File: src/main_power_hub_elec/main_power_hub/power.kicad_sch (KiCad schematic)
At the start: 35 parts, among them J1 XT30M, U220 MP2459GJ-Z-MS, U230 AP62200TWU, U240 HX4002

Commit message: Wire channels on schematic
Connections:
- net VBUS_{SENSE}: now also C12.2, R3.2, R4.1
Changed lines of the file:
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@@
+	)
+	(junction
+		(at 73.66 36.83)
+		(diameter 0)
+		(color 0 0 0 0)
 	)
 	(junction
@@
 		)
 		(stroke
+			(width 0)
+			(type default)
+		)
+	)
+	(wire
+		(pts
+			(xy 73.66 36.83) (xy 76.2 36.83)
+		)
+		(stroke

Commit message: Make the bus real
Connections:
- net +12V: no longer U230.5 (EN)
- net GND: now also D3.2 (A2); no longer D3.1 (A1)
- net VBUS: now also D3.1 (A1); no longer D3.2 (A2)
- no-connect marks 0 -> 1
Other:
- moved on the sheet: D3
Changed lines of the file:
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@@
 	)
 	(junction
-		(at 29.21 81.28)
-		(diameter 0)
-		(color 0 0 0 0)
-	)
-	(junction
 		(at 185.42 39.37)
 		(diameter 0)
@@
 		(color 0 0 0 0)
 	)
+	(no_connect
+		(at 30.48 86.36)
+	)
 	(wire
 		(pts
@@
 	(wire
 		(pts
-			(xy 30.48 86.36) (xy 29.21 86.36)
-		)
-		(stroke
-			(width 0)
-			(type default)
-		)
-	)
-	(wire
-		(pts
 			(xy 34.29 133.35) (xy 36.83 133.35)
 		)
@@
 	(wire
 		(pts
-			(xy 29.21 81.28) (xy 30.48 81.28)
+			(xy 26.67 81.28) (xy 30.48 81.28)
 		)
 		(stroke
@@
 	(wire
 		(pts
-			(xy 29.21 81.28) (xy 29.21 86.36)
-		)
-		(stroke
-			(width 0)
-			(type default)
-		)
-	)
-	(wire
-		(pts
 			(xy 185.42 35.56) (xy 185.42 39.37)
 		)
@@
 	(wire
 		(pts
-			(xy 26.67 81.28) (xy 29.21 81.28)
-		)
-		(stroke
-			(width 0)
-			(type default)
-		)
-	)
-	(wire
-		(pts
 			(xy 195.58 26.67) (xy 199.39 26.67)
 		)
@@
 	(symbol
 		(lib_id "Device:D_TVS_Small")
-		(at 55.88 33.02 90)
+		(at 55.88 33.02 270)
 		(unit 1)
 		(exclude_from_sim no)
@@
 		(dnp no)
 		(property "Reference" "D3"
-			(at 57.912 33.02 90)
+			(at 53.848 33.02 90)
 			(effects
 				(font
@@
 		)
 		(property "Value" "30V"
-			(at 57.912 35.56 90)
+			(at 53.848 30.48 90)
 			(effects
 				(font

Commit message: Schematic done (?)
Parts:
- J1: value XT30M -> XT90M

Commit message: evan made me do it footprints done
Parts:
- C12: footprint (none) -> Capacitor_SMD:C_0402_1005Metric
- D3: footprint (none) -> Diode_SMD:D_SMF
- J1: footprint (none) -> Connector_AMASS:AMASS_XT90PW-M_1x02_P10.90mm_Horizontal
- R3, R4: footprint (none) -> Resistor_SMD:R_0402_1005Metric
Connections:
- net VBUS_{FLT}: no longer U220.4 (EN)
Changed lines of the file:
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@@
 	)
 	(junction
-		(at 148.59 26.67)
-		(diameter 0)
-		(color 0 0 0 0)
-	)
-	(junction
 		(at 190.5 39.37)
 		(diameter 0)
@@
 	(wire
 		(pts
-			(xy 148.59 26.67) (xy 146.05 26.67)
+			(xy 146.05 26.67) (xy 149.86 26.67)
 		)
 		(stroke
@@
 	(wire
 		(pts
-			(xy 148.59 26.67) (xy 149.86 26.67)
-		)
-		(stroke
-			(width 0)
-			(type default)
-		)
-	)
-	(wire
-		(pts
 			(xy 34.29 133.35) (xy 36.83 133.35)
 		)
@@
 	(wire
 		(pts
-			(xy 149.86 31.75) (xy 148.59 31.75)
-		)
-		(stroke
-			(width 0)
-			(type default)
-		)
-	)
-	(wire
-		(pts
 			(xy 58.42 81.28) (xy 58.42 83.82)
 		)
@@
 	(wire
 		(pts
-			(xy 148.59 26.67) (xy 148.59 31.75)
-		)
-		(stroke
-			(width 0)
-			(type default)
-		)
-	)
-	(wire
-		(pts
 			(xy 53.34 86.36) (xy 50.8 86.36)
 		)
@@
 			)
 		)
-		(property "Footprint" ""
+		(property "Footprint" "Capacitor_SMD:C_0402_1005Metric"
 			(at 73.66 43.18 90)
 			(effects
@@
 			)
 		)
-		(property "Footprint" ""
+		(property "Footprint" "Connector_AMASS:AMASS_XT90PW-M_1x02_P10.90mm_Horizontal"
 			(at 30.48 29.21 0)
 			(effects
@@
 			)
 		)
-		(property "Footprint" ""
+		(property "Footprint" "Resistor_SMD:R_0402_1005Metric"
 			(at 67.31 41.91 0)
 			(effects
@@
 			)
 		)
-		(property "Footprint" ""
+		(property "Footprint" "Diode_SMD:D_SMF"
 			(at 55.88 33.02 0)
 			(effects
@@
 			)
 		)
-		(property "Footprint" ""
+		(property "Footprint" "Resistor_SMD:R_0402_1005Metric"
 			(at 67.31 33.02 0)
 			(effects

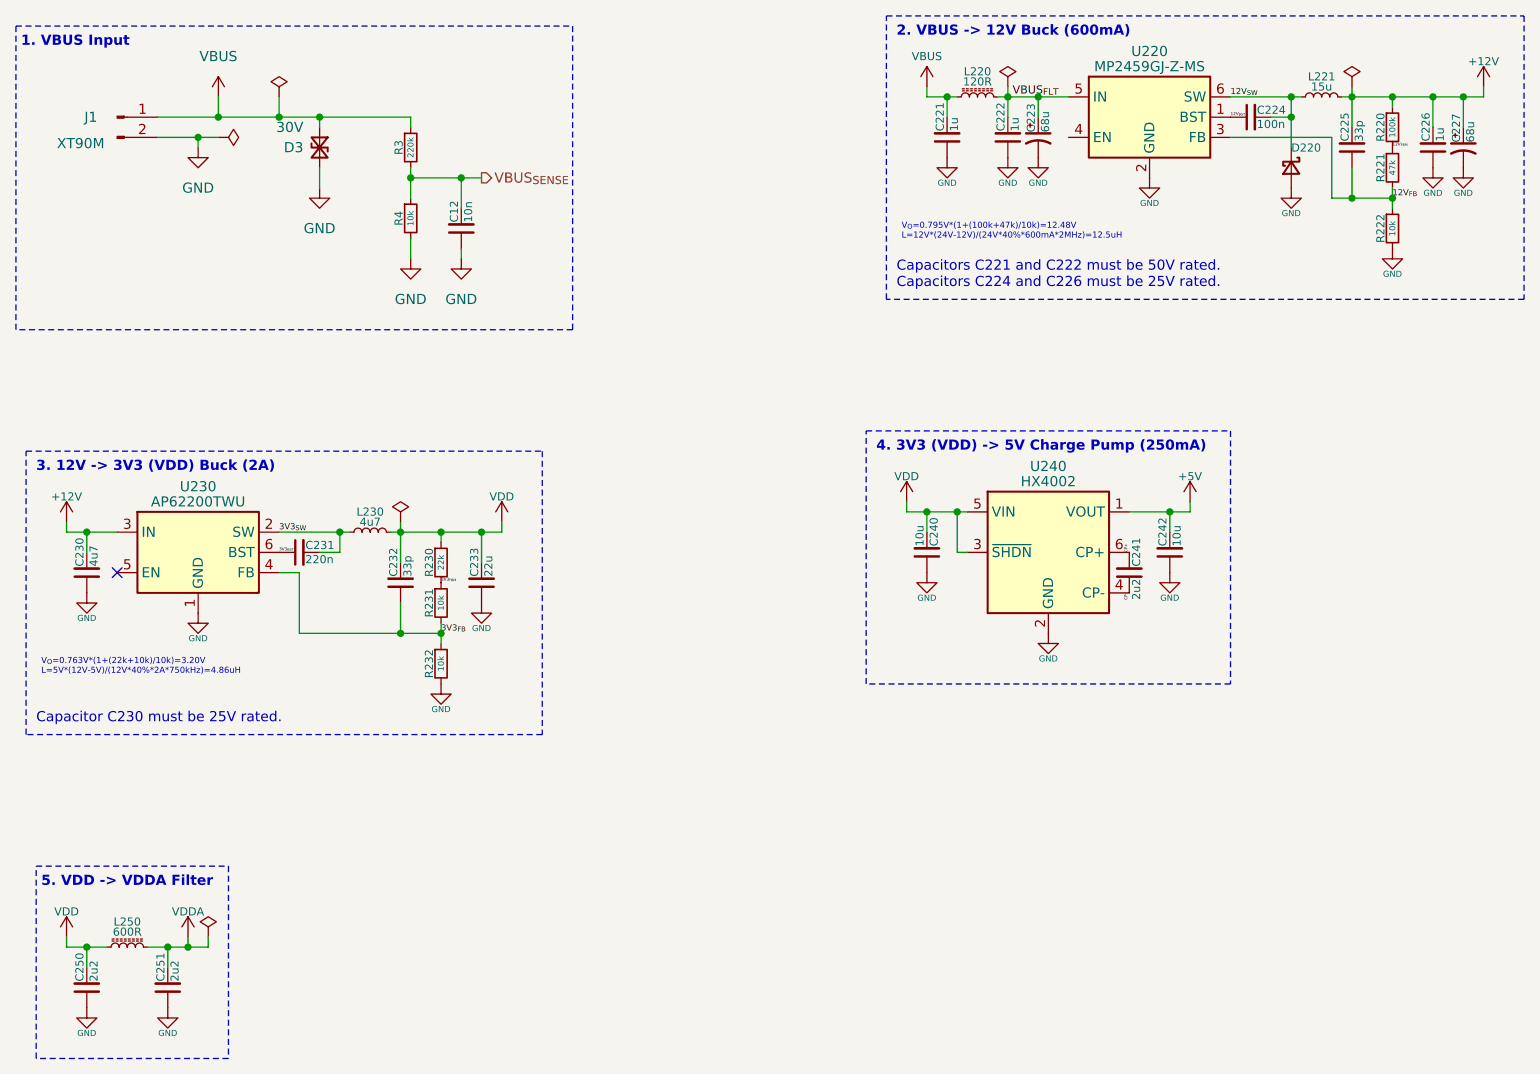
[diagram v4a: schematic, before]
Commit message: FULL LAYOUT DONE need traces
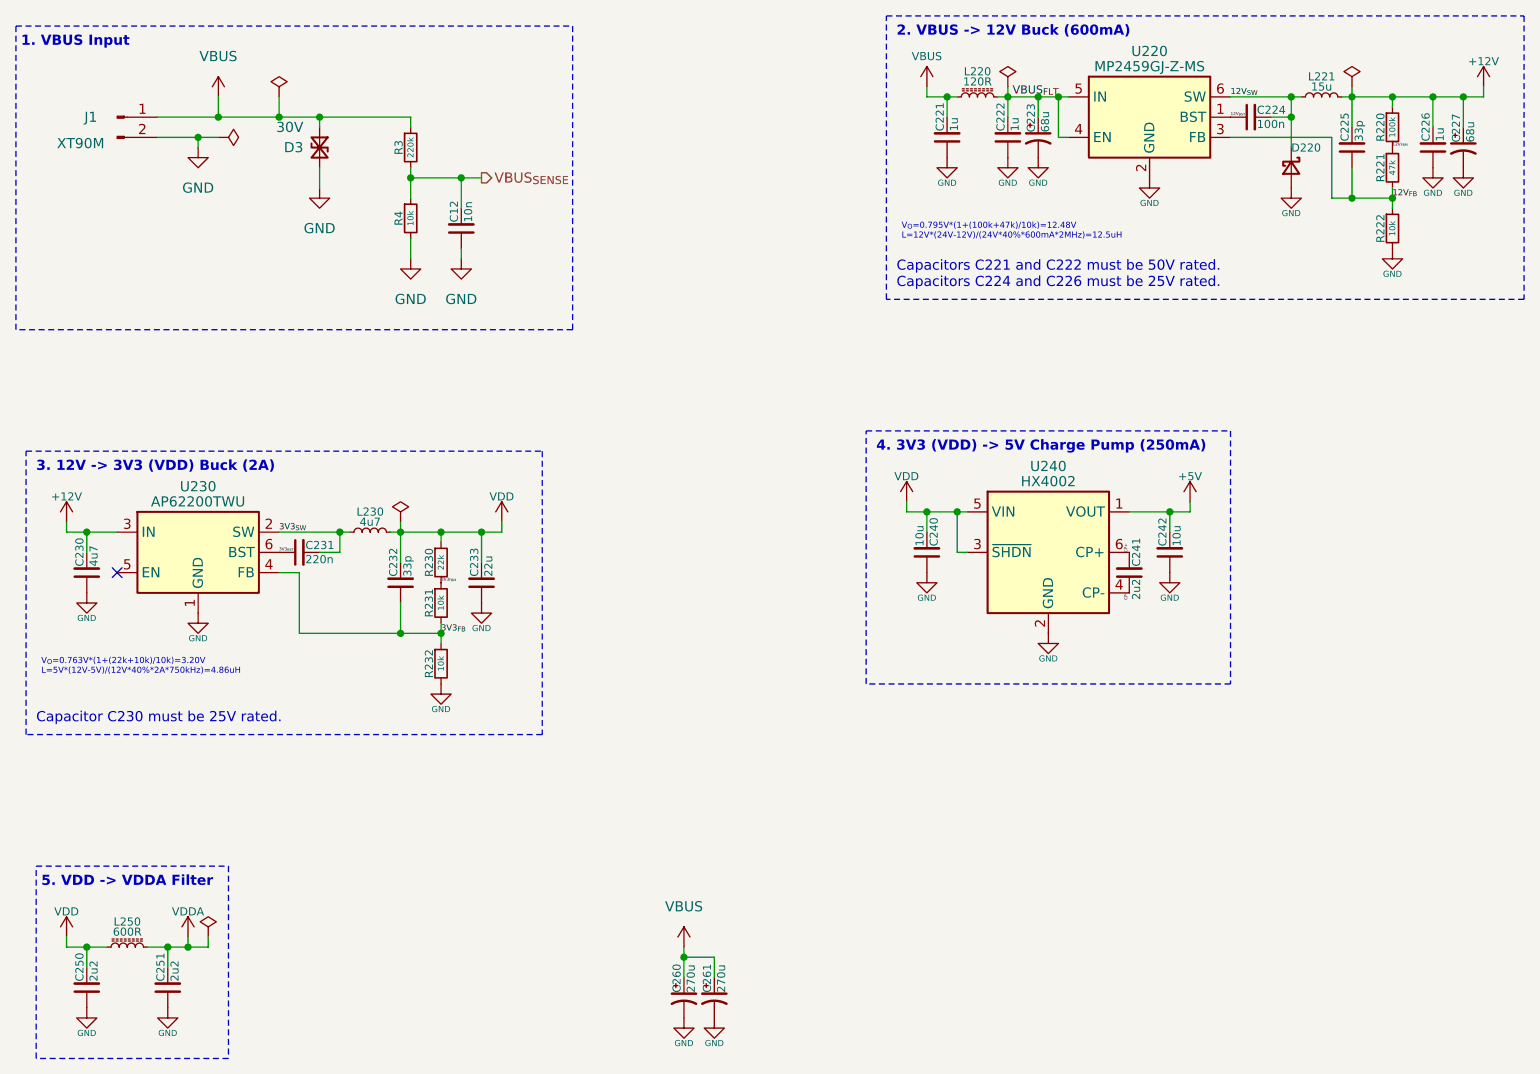
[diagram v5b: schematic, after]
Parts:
- added C260, C261: 270u, Capacitor_SMD:CP_Elec_10x10, symbol Device:C_Polarized_Small_US
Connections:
- net +12V: now also L221.1; no longer L221.2
- net 12V_{SW}: now also L221.2; no longer L221.1
- net GND: now also C260.2, C261.2
- net VBUS: now also C260.1, C261.1
- net VBUS_{FLT}: now also U220.4 (EN)
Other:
- moved on the sheet: L221
